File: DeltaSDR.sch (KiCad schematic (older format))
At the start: 52 parts, among them J1 Conn_01x03_Male, J2 Conn_01x05_Male, J3 Barrel_Jack, J4 USB_A, U1 TC1262-33, U2 Si570, U4 PCM3060, U5 CY8C3246PVI-147, U6 TC1262-5, U7 TC1262-5, U8 74HC74, Y1 Crystal_GND24

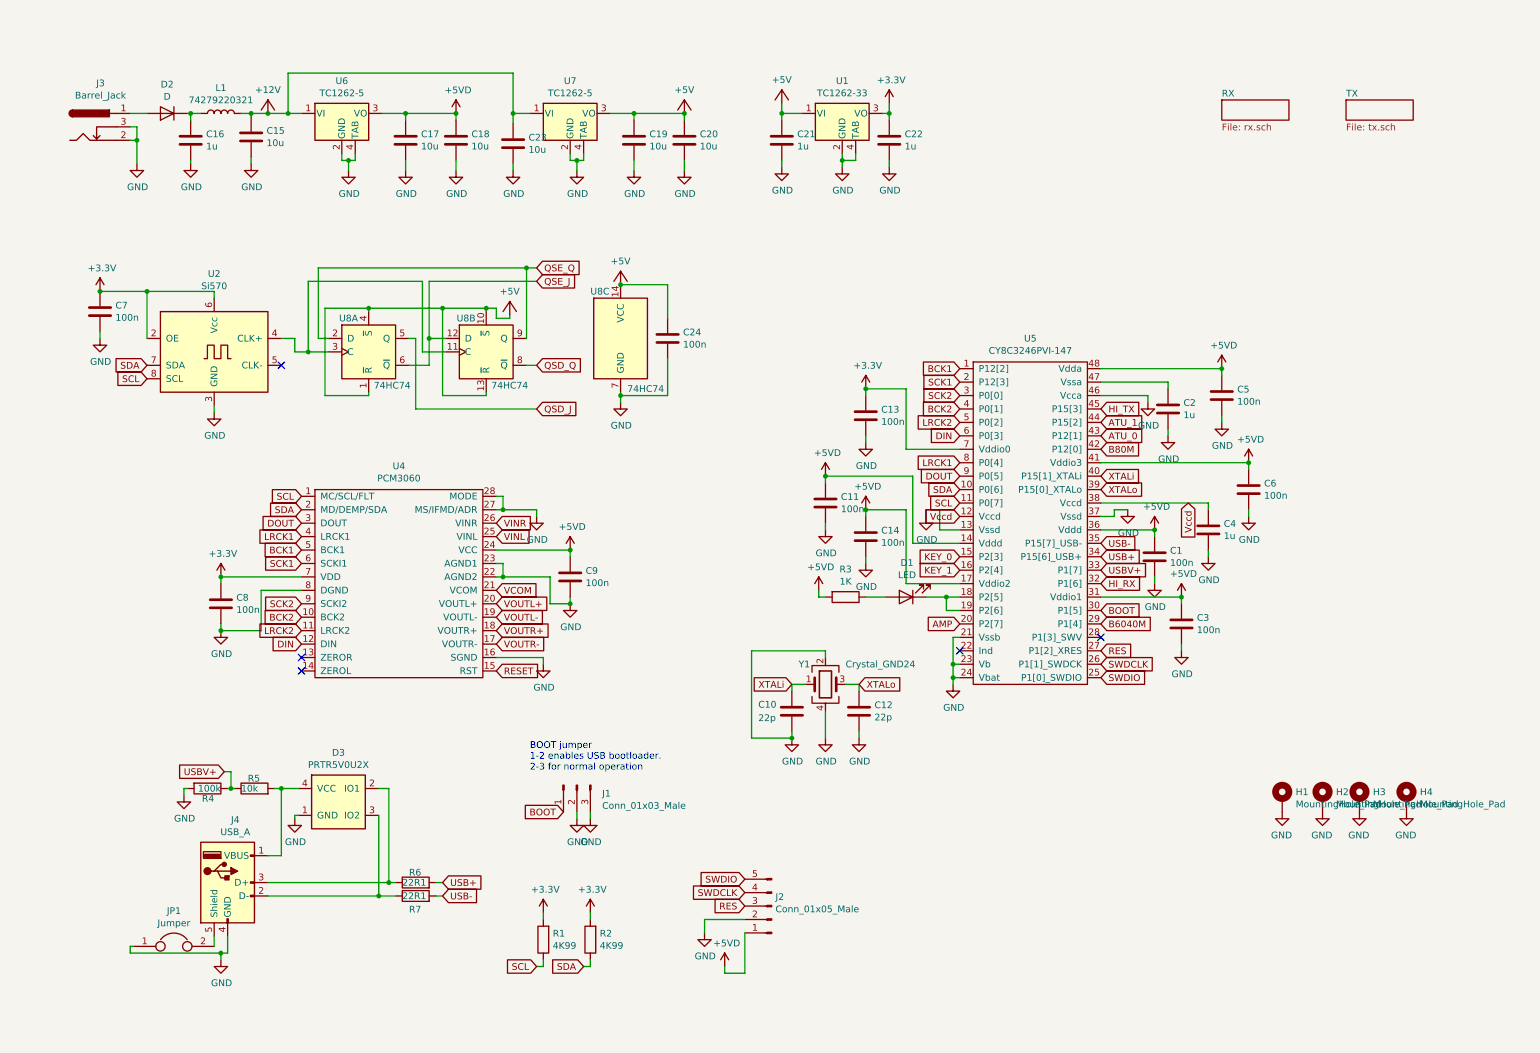
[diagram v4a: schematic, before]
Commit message: ERC, DRC done, added output for ATU and AMP
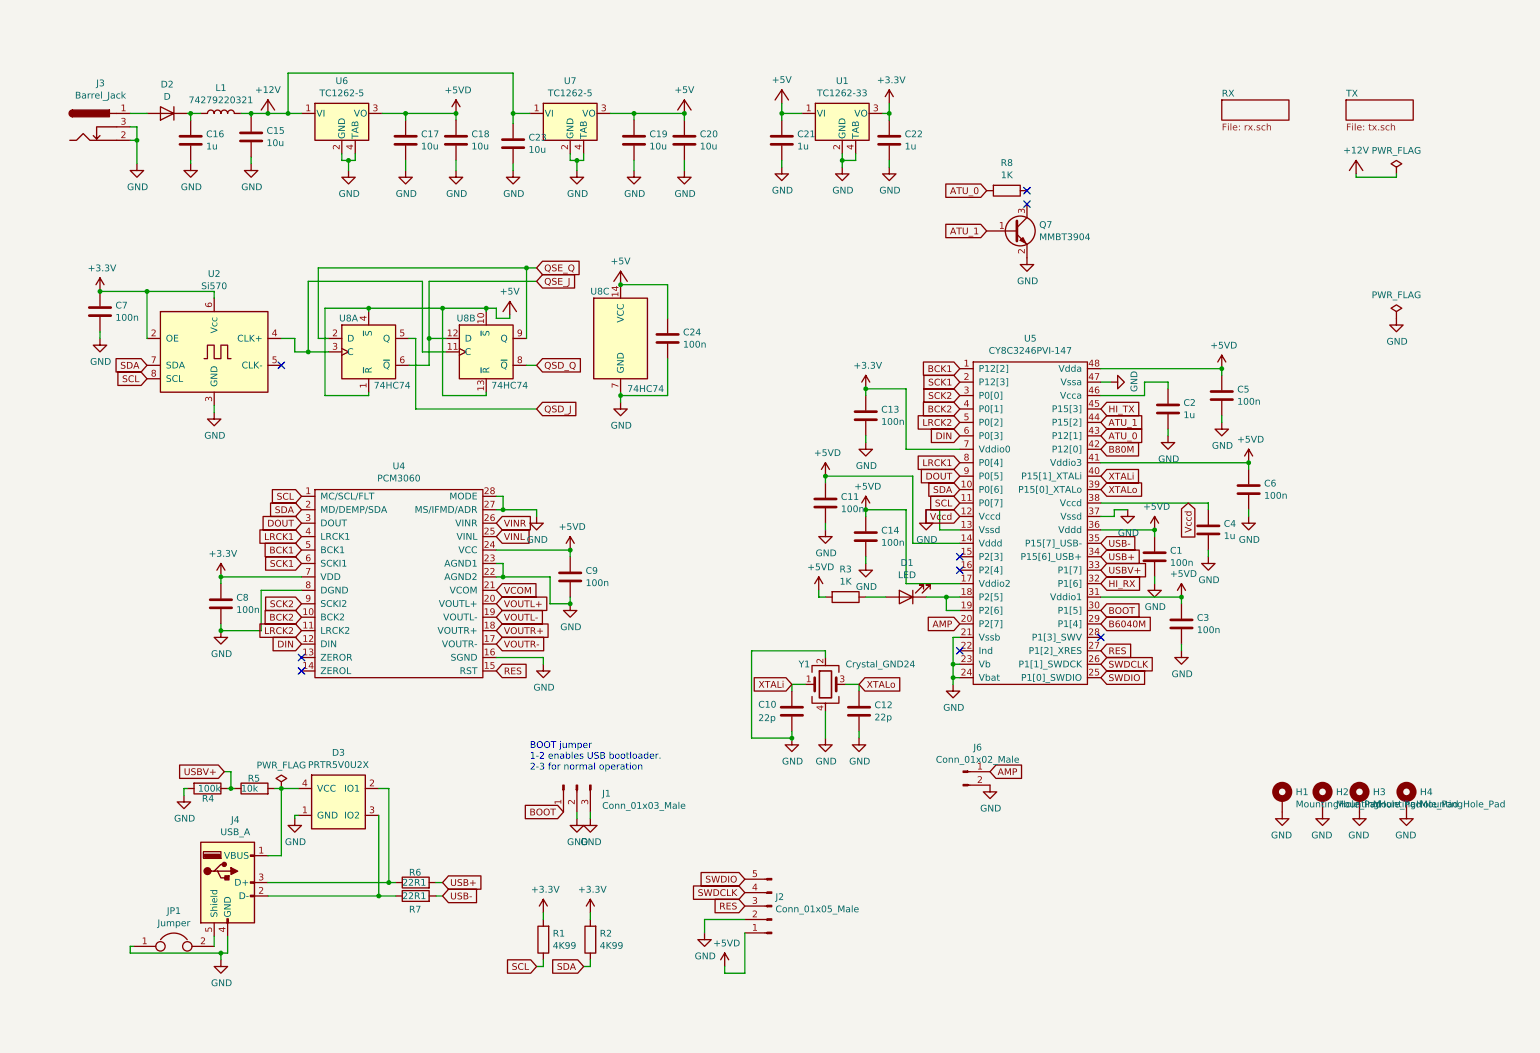
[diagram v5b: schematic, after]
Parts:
- added J6: Conn_01x02_Male, Connector_PinSocket_2.54mm:PinSocket_1x02_P2.54mm_Vertical_SMD_Pin1Right, symbol Connector:Conn_01x02_Male
- added Q7: MMBT3904, Package_TO_SOT_SMD:SOT-23, symbol Transistor_BJT:MMBT3904
- added R8: 1K, Resistor_SMD:R_0603_1608Metric, symbol DeltaSDR-rescue:R-Device-DeltaSDR-rescue
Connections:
- net RESET is gone; now on net RES: U4.15 (RST)
- net AMP: now also J6.1 (Pin_1)
- net ATU_0: now also R8.2
- net ATU_1: now also Q7.1 (B)
- net GND: now also U5.47 (Vssa), J6.2 (Pin_2), Q7.2 (E); no longer U5.46 (Vcca)
- net at C2.1: now also U5.46 (Vcca); no longer U5.47 (Vssa)
- net KEY_0: no longer names the net of U5.15 (P2[3])
- net KEY_1: no longer names the net of U5.16 (P2[4])
- no-connect marks 5 -> 9
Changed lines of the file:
@@
 L power:GND #PWR0106
 U 1 1 5E8C7715
-P 8950 3100
-F 0 "#PWR0106" H 8950 2850 50  0001 C CNN
-F 1 "GND" H 8955 2927 50  0000 C CNN
-F 2 "" H 8950 3100 50  0001 C CNN
-F 3 "" H 8950 3100 50  0001 C CNN
-	1    8950 3100
-	1    0    0    -1
-$EndComp
-Wire Wire Line
-	8600 3050 8950 3050
-Wire Wire Line
-	8950 3050 8950 3100
-Wire Wire Line
-	8600 2950 9100 2950
+P 8675 2950
+F 0 "#PWR0106" H 8675 2700 50  0001 C CNN
+F 1 "GND" H 8680 2777 50  0000 C CNN
+F 2 "" H 8675 2950 50  0001 C CNN
+F 3 "" H 8675 2950 50  0001 C CNN
+	1    8675 2950
+	0    -1   -1   0
+$EndComp
 Wire Wire Line
 	8600 2850 9500 2850
@@
 	1    0    0    -1
 $EndComp
-Text GLabel 7550 4350 0    50   Input ~ 0
-KEY_1
-Text GLabel 7550 4250 0    50   Input ~ 0
-KEY_0
 Wire Wire Line
 	7150 3900 6850 3900
@@
 VOUTR-
 Text GLabel 4100 5100 2    50   Input ~ 0
-RESET
+RES
 $Comp
 L power:GND #PWR0124
@@
 Wire Wire Line
 	3000 1300 3050 1300
+$Comp
+L Transistor_BJT:MMBT3904 Q7
+U 1 1 5E95637E
+P 7950 1825
+F 0 "Q7" H 8141 1871 50  0000 L CNN
+F 1 "MMBT3904" H 8141 1780 50  0000 L CNN
+F 2 "Package_TO_SOT_SMD:SOT-23" H 8150 1750 50  0001 L CIN
+F 3 "https://www.fairchildsemi.com/datasheets/2N/2N3904.pdf" H 7950 1825 50  0001 L CNN
+	1    7950 1825
+	1    0    0    -1
+$EndComp
+$Comp
+L DeltaSDR-rescue:R-Device-DeltaSDR-rescue R8
+U 1 1 5E957013
+P 7900 1525
+F 0 "R8" V 7693 1525 50  0000 C CNN
+F 1 "1K" V 7784 1525 50  0000 C CNN
+F 2 "Resistor_SMD:R_0603_1608Metric" V 7830 1525 50  0001 C CNN
+F 3 "~" H 7900 1525 50  0001 C CNN
+	1    7900 1525
+	0    1    1    0
+$EndComp
+Text GLabel 7750 1825 0    50   Input ~ 0
+ATU_1
+Text GLabel 7750 1525 0    50   Input ~ 0
+ATU_0
+$Comp
+L power:GND #PWR0226
+U 1 1 5E968E1F
+P 8050 2025
+F 0 "#PWR0226" H 8050 1775 50  0001 C CNN
+F 1 "GND" H 8055 1852 50  0000 C CNN
+F 2 "" H 8050 2025 50  0001 C CNN
+F 3 "" H 8050 2025 50  0001 C CNN
+	1    8050 2025
+	1    0    0    -1
+$EndComp
+NoConn ~ 8050 1525
+NoConn ~ 8050 1625
+$Comp
+L power:PWR_FLAG #FLG0101
+U 1 1 5E97A317
+P 10800 1400
+F 0 "#FLG0101" H 10800 1475 50  0001 C CNN
+F 1 "PWR_FLAG" H 10800 1573 50  0000 C CNN
+F 2 "" H 10800 1400 50  0001 C CNN
+F 3 "~" H 10800 1400 50  0001 C CNN
+	1    10800 1400
+	1    0    0    -1
+$EndComp
+$Comp
+L DeltaSDR-rescue:+12V-mdSupply #PWR0227
+U 1 1 5E97AD8C
+P 10500 1300
+F 0 "#PWR0227" H 10500 1300 50  0001 C BNN
+F 1 "+12V" H 10500 1375 50  0000 C CNN
+F 2 "" H 10500 1300 50  0001 C CNN
+F 3 "" H 10500 1300 50  0001 C CNN
+	1    10500 1300
+	1    0    0    -1
+$EndComp
+Wire Wire Line
+	10500 1400 10500 1425
+Wire Wire Line
+	10500 1425 10800 1425
+Wire Wire Line
+	10800 1425 10800 1400
+$Comp
+L power:GND #PWR0231
+U 1 1 5EA118EE
+P 10800 2475
+F 0 "#PWR0231" H 10800 2225 50  0001 C CNN
+F 1 "GND" H 10805 2302 50  0000 C CNN
+F 2 "" H 10800 2475 50  0001 C CNN
+F 3 "" H 10800 2475 50  0001 C CNN
+	1    10800 2475
+	1    0    0    -1
+$EndComp
+$Comp
+L power:PWR_FLAG #FLG0105
+U 1 1 5EA12091
+P 10800 2475
+F 0 "#FLG0105" H 10800 2550 50  0001 C CNN
+F 1 "PWR_FLAG" H 10800 2648 50  0000 C CNN
+F 2 "" H 10800 2475 50  0001 C CNN
+F 3 "~" H 10800 2475 50  0001 C CNN
+	1    10800 2475
+	1    0    0    -1
+$EndComp
+NoConn ~ 7550 4250
+NoConn ~ 7550 4350
+$Comp
+L power:PWR_FLAG #FLG0102
+U 1 1 5EA6D656
+P 2500 5975
+F 0 "#FLG0102" H 2500 6050 50  0001 C CNN
+F 1 "PWR_FLAG" H 2500 6148 50  0000 C CNN
+F 2 "" H 2500 5975 50  0001 C CNN
+F 3 "~" H 2500 5975 50  0001 C CNN
+	1    2500 5975
+	1    0    0    -1
+$EndComp
+Wire Wire Line
+	8600 2950 8675 2950
+Wire Wire Line
+	8600 3050 8925 3050
+Wire Wire Line
+	8925 3050 8925 2950
+Wire Wire Line
+	8925 2950 9100 2950
+$Comp
+L Connector:Conn_01x02_Male J6
+U 1 1 5EB03FAC
+P 7575 5850
+F 0 "J6" H 7683 6031 50  0000 C CNN
+F 1 "Conn_01x02_Male" H 7683 5940 50  0000 C CNN
+F 2 "Connector_PinSocket_2.54mm:PinSocket_1x02_P2.54mm_Vertical_SMD_Pin1Right" H 7575 5850 50  0001 C CNN
+F 3 "~" H 7575 5850 50  0001 C CNN
+	1    7575 5850
+	1    0    0    -1
+$EndComp
+Text GLabel 7775 5850 2    50   Input ~ 0
+AMP
+$Comp
+L power:GND #PWR0230
+U 1 1 5EB0481E
+P 7775 5950
+F 0 "#PWR0230" H 7775 5700 50  0001 C CNN
+F 1 "GND" H 7780 5777 50  0000 C CNN
+F 2 "" H 7775 5950 50  0001 C CNN
+F 3 "" H 7775 5950 50  0001 C CNN
+	1    7775 5950
+	1    0    0    -1
+$EndComp
 $EndSCHEMATC

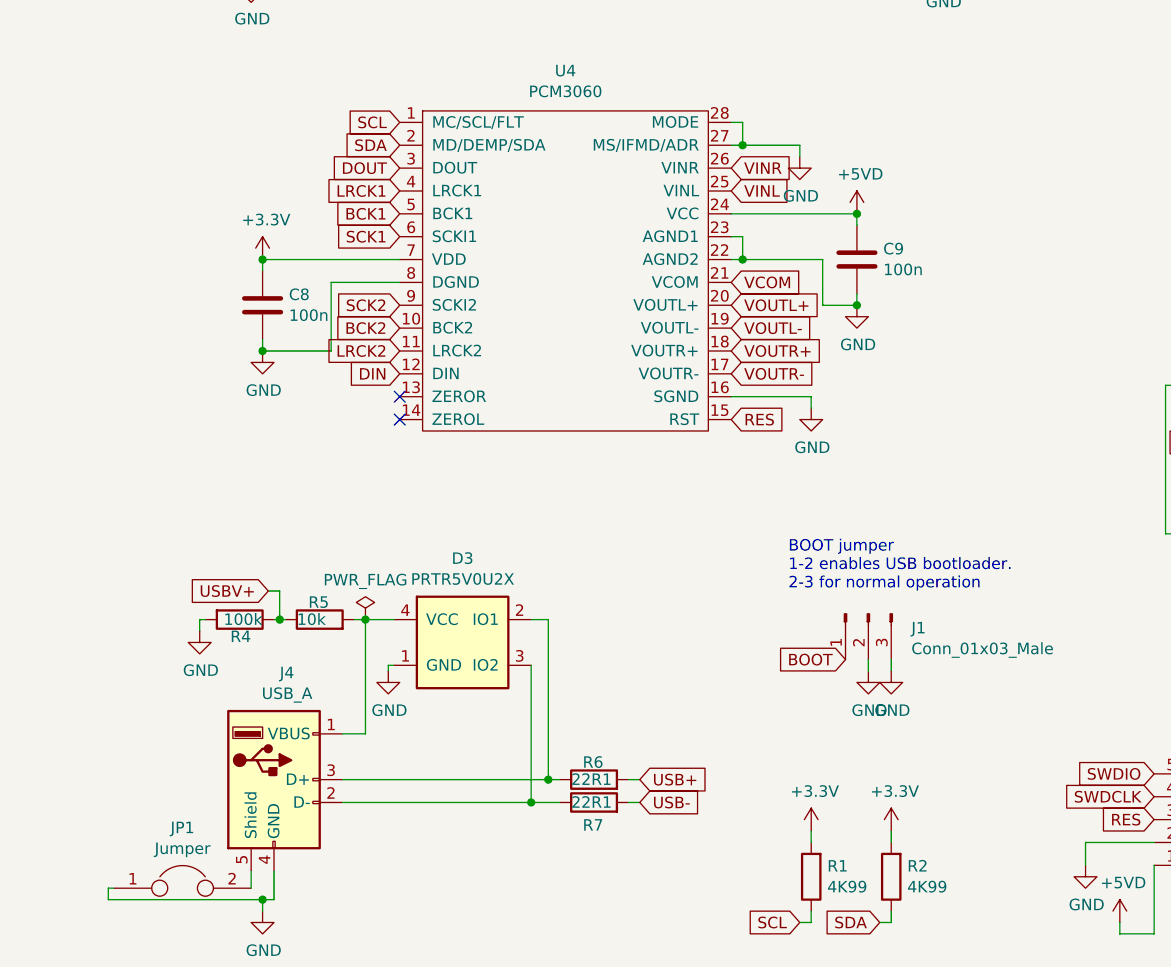
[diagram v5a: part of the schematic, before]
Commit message: PCM3060 suplied from different voltage rail. Improved ground separation and USB layout
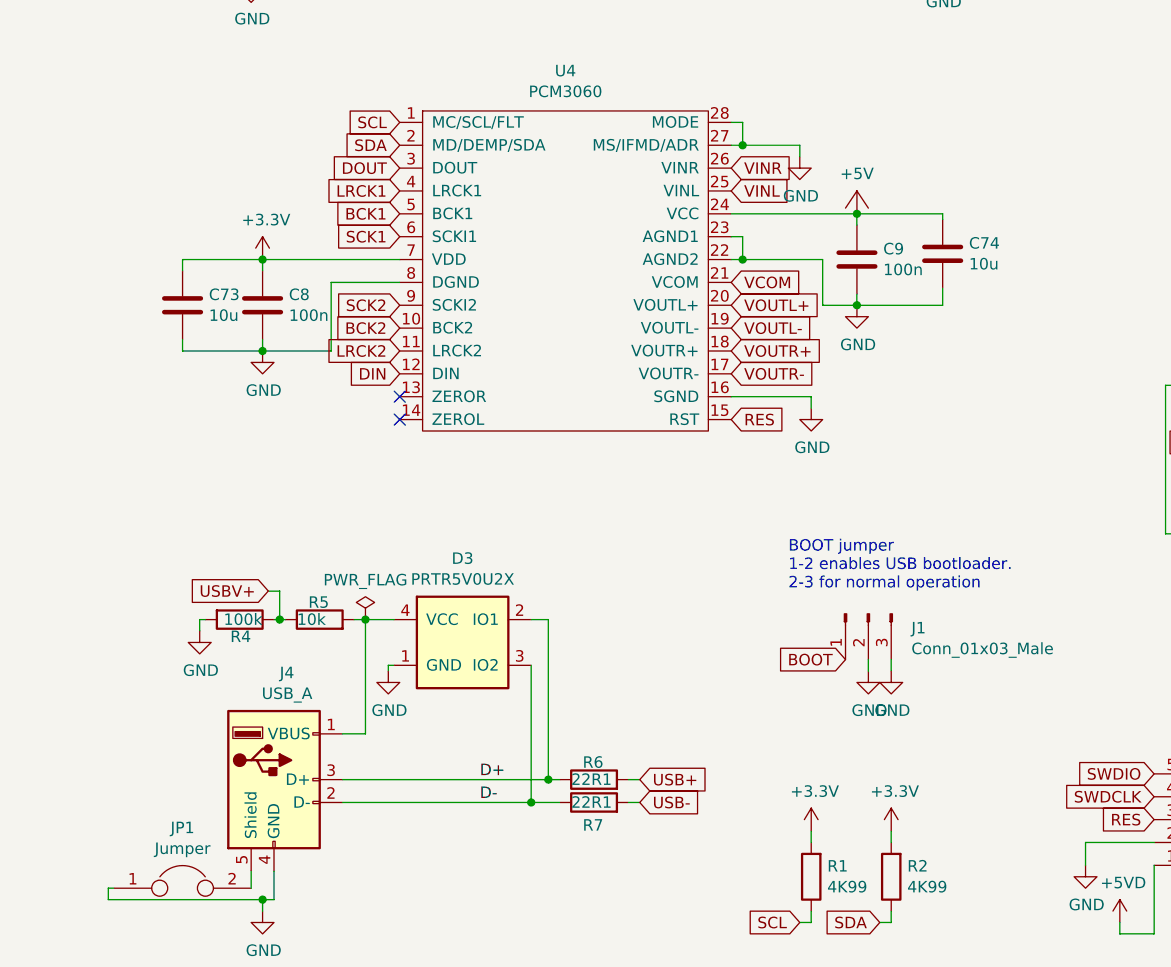
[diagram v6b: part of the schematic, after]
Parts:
- added C73, C74: 10u, Capacitor_SMD:C_0805_2012Metric, symbol DeltaSDR-rescue:C-Device-DeltaSDR-rescue
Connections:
- net +3V3: now also C73.1
- net +5V: now also C9.1, U4.24 (VCC), C74.1
- net +5VD: no longer C9.1, U4.24 (VCC)
- net GND: now also C73.2, C74.2
- net D-: now reaches D3.3 (IO2), J4.2 (D-), R7.1
- net D+: now reaches D3.2 (IO1), J4.3 (D+), R6.1
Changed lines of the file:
@@
 Wire Wire Line
 	4650 4550 4650 4600
-$Comp
-L power:+5VD #PWR0123
-U 1 1 5E8FBE4D
-P 4650 4200
-F 0 "#PWR0123" H 4650 4050 50  0001 C CNN
-F 1 "+5VD" H 4665 4373 50  0000 C CNN
-F 2 "" H 4650 4200 50  0001 C CNN
-F 3 "" H 4650 4200 50  0001 C CNN
-	1    4650 4200
-	1    0    0    -1
-$EndComp
 Wire Wire Line
 	4100 4200 4650 4200
-Connection ~ 4650 4200
 Wire Wire Line
 	4100 4300 4150 4300
@@
 	1    0    0    -1
 $EndComp
+$Comp
+L DeltaSDR-rescue:+5V-mdSupply #PWR0123
+U 1 1 5E985F11
+P 4650 4100
+F 0 "#PWR0123" H 4650 4100 50  0001 C BNN
+F 1 "+5V" H 4650 4175 50  0000 C CNN
+F 2 "" H 4650 4100 50  0001 C CNN
+F 3 "" H 4650 4100 50  0001 C CNN
+	1    4650 4100
+	1    0    0    -1
+$EndComp
+Connection ~ 4650 4200
+$Comp
+L DeltaSDR-rescue:C-Device-DeltaSDR-rescue C73
+U 1 1 5E9BAD69
+P 1700 4600
+F 0 "C73" H 1815 4646 50  0000 L CNN
+F 1 "10u" H 1815 4555 50  0000 L CNN
+F 2 "Capacitor_SMD:C_0805_2012Metric" H 1738 4450 50  0001 C CNN
+F 3 "~" H 1700 4600 50  0001 C CNN
+	1    1700 4600
+	1    0    0    -1
+$EndComp
+$Comp
+L DeltaSDR-rescue:C-Device-DeltaSDR-rescue C74
+U 1 1 5E9BB43C
+P 5025 4375
+F 0 "C74" H 5140 4421 50  0000 L CNN
+F 1 "10u" H 5140 4330 50  0000 L CNN
+F 2 "Capacitor_SMD:C_0805_2012Metric" H 5063 4225 50  0001 C CNN
+F 3 "~" H 5025 4375 50  0001 C CNN
+	1    5025 4375
+	1    0    0    -1
+$EndComp
+Wire Wire Line
+	4650 4200 5025 4200
+Wire Wire Line
+	5025 4200 5025 4225
+Wire Wire Line
+	4650 4600 5025 4600
+Wire Wire Line
+	5025 4600 5025 4525
+Wire Wire Line
+	2050 4400 1700 4400
+Wire Wire Line
+	1700 4400 1700 4450
+Wire Wire Line
+	2050 4800 1700 4800
+Wire Wire Line
+	1700 4800 1700 4750
+Text Label 3000 6675 0    50   ~ 0
+D+
+Text Label 3000 6775 0    50   ~ 0
+D-
 $EndSCHEMATC

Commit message: Corrected Q6 connection, RX schematic clean up
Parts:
- H1, H2, H3, H4: symbol Mechanical:MountingHole_Pad -> DeltaSDR-rescue:MountingHole_Pad-Mechanical
- JP1: symbol Device:Jumper -> DeltaSDR-rescue:Jumper-Device
- Q7: symbol Transistor_BJT:MMBT3904 -> DeltaSDR-rescue:MMBT3904-Transistor_BJT
- Y1: symbol Device:Crystal_GND24 -> DeltaSDR-rescue:Crystal_GND24-Device
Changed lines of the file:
@@
 EESchema Schematic File Version 4
-LIBS:DeltaSDR-cache
-EELAYER 29 0
+EELAYER 30 0
 EELAYER END
 $Descr A4 11693 8268
@@
 	2400 950  2550 950
 $Comp
-L Device:Crystal_GND24 Y1
+L DeltaSDR-rescue:Crystal_GND24-Device Y1
 U 1 1 5E9781A4
 P 6550 5200
@@
 B6040M
 $Comp
-L Device:Jumper JP1
+L DeltaSDR-rescue:Jumper-Device JP1
 U 1 1 5EA337DB
 P 1700 7150
@@
 Connection ~ 2050 7200
 $Comp
-L Mechanical:MountingHole_Pad H?
+L DeltaSDR-rescue:MountingHole_Pad-Mechanical H?
 U 1 1 5EAFAA06
 P 10875 6050
@@
 $EndComp
 $Comp
-L Mechanical:MountingHole_Pad H?
+L DeltaSDR-rescue:MountingHole_Pad-Mechanical H?
 U 1 1 5EAFAA12
 P 10525 6050
@@
 $EndComp
 $Comp
-L Mechanical:MountingHole_Pad H?
+L DeltaSDR-rescue:MountingHole_Pad-Mechanical H?
 U 1 1 5EAFAA1E
 P 10250 6050
@@
 $EndComp
 $Comp
-L Mechanical:MountingHole_Pad H?
+L DeltaSDR-rescue:MountingHole_Pad-Mechanical H?
 U 1 1 5EAFAA2A
 P 9950 6050
@@
 	3000 1300 3050 1300
 $Comp
-L Transistor_BJT:MMBT3904 Q7
+L DeltaSDR-rescue:MMBT3904-Transistor_BJT Q7
 U 1 1 5E95637E
 P 7950 1825
